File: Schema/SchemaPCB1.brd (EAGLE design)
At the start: 63.9 x 71.4 mm, 31 parts, among them J1 CON-HIROSE-COAXIAL-U.FL, J2 Programmer, J4 39700-0205, J5 39700-0002, U1 RN2483, U2 TPS22860DBVR, U3 ESP32, U4 SOT-89-5, U5 SI7217-B-01-IVR, U6 TPS22860DBVR

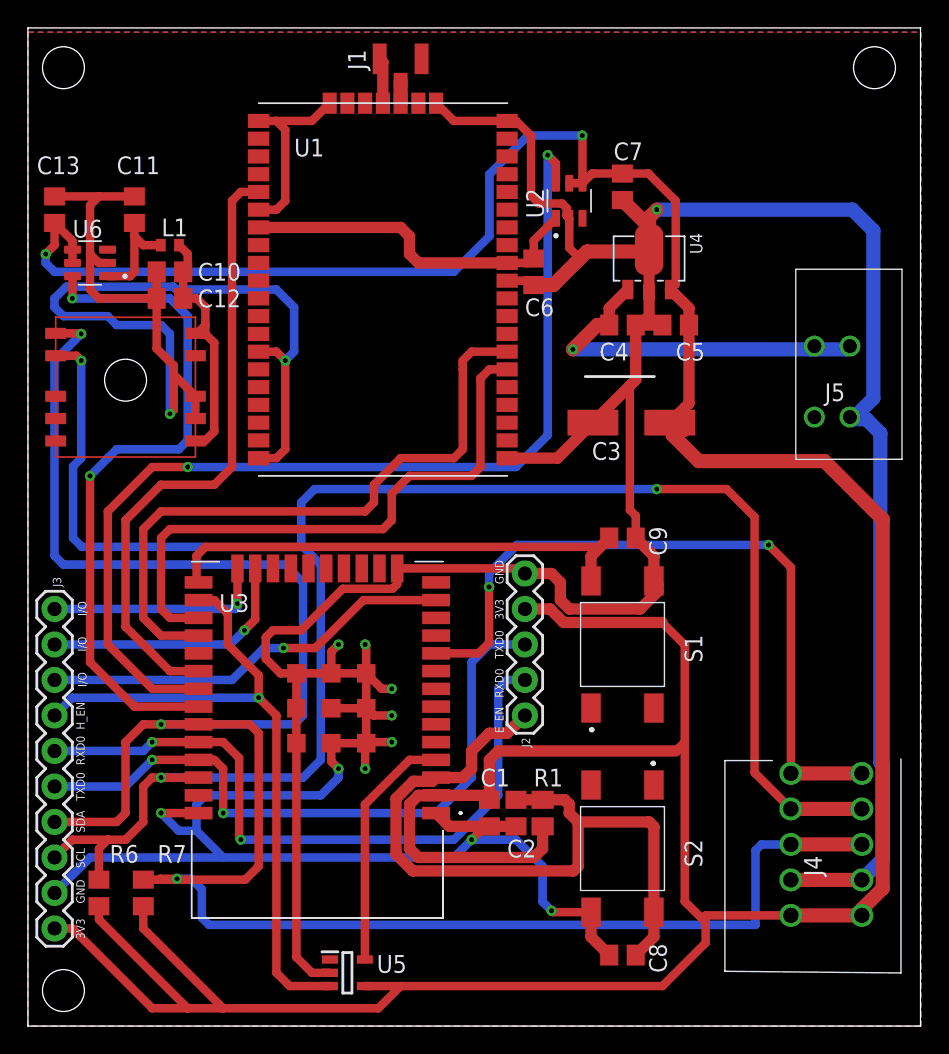
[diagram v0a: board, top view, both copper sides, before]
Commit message: aangepast om te gebruiken met gps breakout board
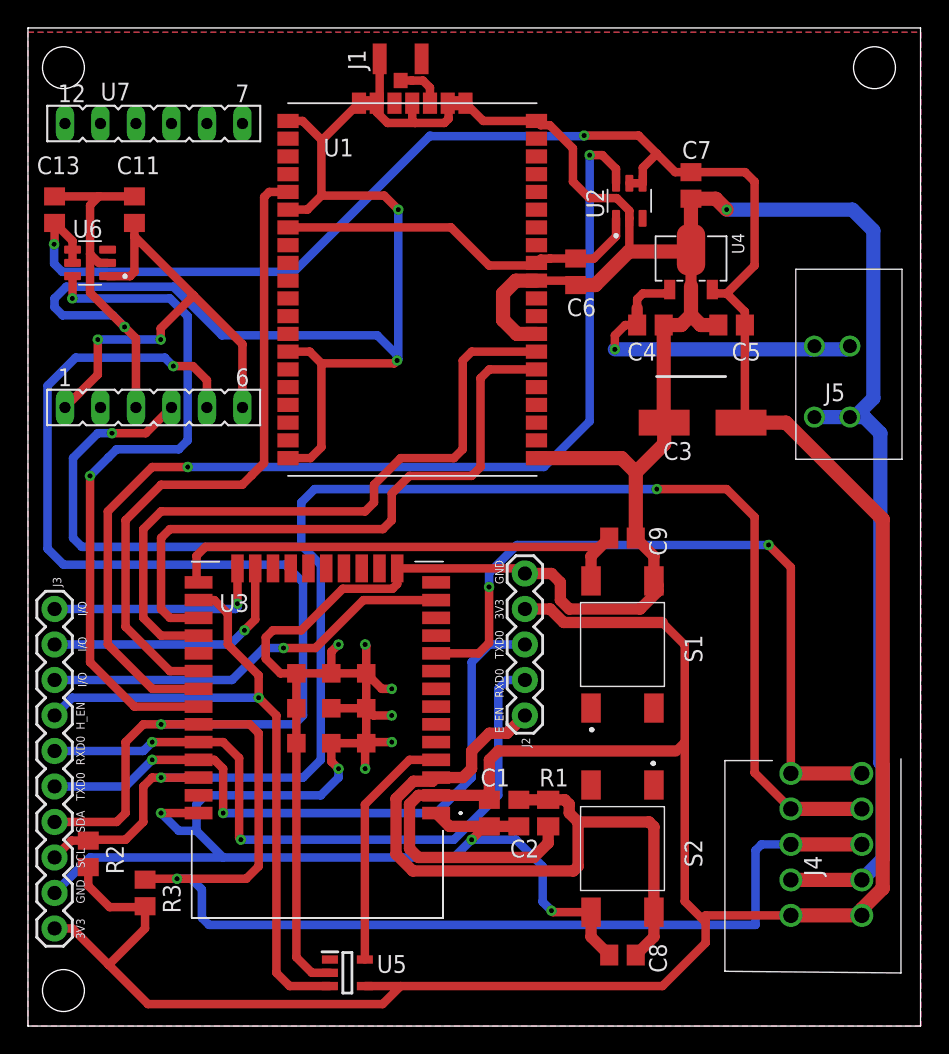
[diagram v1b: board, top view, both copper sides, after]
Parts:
- removed C10, C12: (no value), rcl:C0805
- removed L1: BLM15HB121SN1, inductors:0402
- removed R6, R7: (no value), rcl:R0805
- removed U?1: GPS, gps:GPS
- added R2, R3: (no value), rcl:R0805
- added U7: ADAFRUIT_MINIGPS, gps:ADAFRUIT_MINIGPS
- moved C3 5.10 mm to (48.3, 71.8)
- moved C7 4.90 mm to (47.4, 88.7)
- moved U2 4.30 mm to (43.0, 87.6)
- moved C5 4.00 mm to (50.4, 78.7)
- moved C6 3.00 mm to (39.2, 82.5)
- moved U4 3.00 mm to (47.5, 83.2)
- moved U1 2.10 mm to (18.6, 67.9)
- moved C4 2.00 mm to (44.5, 78.7)
- moved R1 0.40 mm to (37.2, 43.8)
- moved C2 0.20 mm to (35.1, 43.8)
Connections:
- removed net N$6: C10.1, C12.1, L1.1, U?1.NRESET, U?1.VCC
- removed net N$7: C11.1, L1.2, U6.1
- new net GPS_EN: C11.1, U6.1, U7.1, U7.6
- net +3V3: now also R2.2, R3.2; no longer R6.2, R7.2
- net GND: now also U7.3; no longer C10.2, C12.2, U?1.GND, U?1.WAKE-UP
- net I2C_SCL: now also R2.1, U7.4; no longer R6.1, U?1.I2C_SCL
- net I2C_SDA: now also R3.1, U7.5; no longer R7.1, U?1.I2C_SDA
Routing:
- net GPS_EN: track 0.00 -> 35.5 mm, vias 0 -> 2
- net GND: track 409.7 -> 437.7 mm, vias 13 -> 14
- net N$6: track 18.2 -> 0.00 mm
- net +3V3: track 287.7 -> 276.6 mm
- net N$7: track 7.70 -> 0.00 mm
- net I2C_SDA: track 154.3 -> 161.6 mm
- net I2C_SCL: track 140.5 -> 136.8 mm
- net RN2483_ENABLE: track 73.4 -> 76.9 mm
- net RXD2: track 42.6 -> 44.7 mm
- net TXD2: track 46.6 -> 48.7 mm
- net RN2483_RESET: track 44.6 -> 46.7 mm
- net BAT_IN: track 26.6 -> 24.6 mm
- net N$4: track 1.62 -> 3.43 mm
- net RN2483_VDD: track 25.1 -> 26.8 mm

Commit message: gerber files geexporteerd
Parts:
- C11: value (none) -> 100nF
- C13: value (none) -> 1uF
- R2, R3: value (none) -> 10k
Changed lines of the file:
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@@
 <attribute name="PURCHASE-URL" value="https://pricing.snapeda.com/search/part/TPS22860DBVR/?ref=eda" x="4.445" y="83.185" size="1.778" layer="27" rot="R180" display="off"/>
 </element>
-<element name="C11" library="rcl" library_urn="urn:adsk.eagle:library:334" package="C0805" package3d_urn="urn:adsk.eagle:package:23617/2" value="" x="7.62" y="86.995" smashed="yes" rot="R90">
+<element name="C11" library="rcl" library_urn="urn:adsk.eagle:library:334" package="C0805" package3d_urn="urn:adsk.eagle:package:23617/2" value="100nF" x="7.62" y="86.995" smashed="yes" rot="R90">
 <attribute name="NAME" x="6.35" y="89.535" size="1.27" layer="25"/>
 <attribute name="POPULARITY" value="88" x="7.62" y="86.995" size="1.778" layer="27" rot="R90" display="off"/>
@@
 <attribute name="VALUE" x="10.16" y="85.725" size="1.27" layer="27" rot="R90"/>
 </element>
-<element name="C13" library="rcl" library_urn="urn:adsk.eagle:library:334" package="C0805" package3d_urn="urn:adsk.eagle:package:23617/2" value="" x="1.905" y="86.995" smashed="yes" rot="R90">
+<element name="C13" library="rcl" library_urn="urn:adsk.eagle:library:334" package="C0805" package3d_urn="urn:adsk.eagle:package:23617/2" value="1uF" x="1.905" y="86.995" smashed="yes" rot="R90">
 <attribute name="NAME" x="0.635" y="89.535" size="1.27" layer="25"/>
 <attribute name="POPULARITY" value="88" x="1.905" y="86.995" size="1.778" layer="27" rot="R90" display="off"/>
@@
 <attribute name="NAME" x="57.7476" y="73.9314" size="1.27" layer="25" align="center"/>
 </element>
-<element name="R2" library="rcl" library_urn="urn:adsk.eagle:library:334" package="R0805" package3d_urn="urn:adsk.eagle:package:23553/2" value="" x="4.318" y="40.894" smashed="yes" rot="R270">
+<element name="R2" library="rcl" library_urn="urn:adsk.eagle:library:334" package="R0805" package3d_urn="urn:adsk.eagle:package:23553/2" value="10k" x="4.318" y="40.894" smashed="yes" rot="R270">
 <attribute name="NAME" x="5.588" y="41.529" size="1.27" layer="25" rot="R270"/>
 <attribute name="POPULARITY" value="86" x="4.318" y="40.894" size="1.778" layer="27" rot="R270" display="off"/>
@@
 <attribute name="VALUE" x="1.778" y="41.529" size="1.27" layer="27" rot="R270"/>
 </element>
-<element name="R3" library="rcl" library_urn="urn:adsk.eagle:library:334" package="R0805" package3d_urn="urn:adsk.eagle:package:23553/2" value="" x="8.382" y="38.1" smashed="yes" rot="R270">
+<element name="R3" library="rcl" library_urn="urn:adsk.eagle:library:334" package="R0805" package3d_urn="urn:adsk.eagle:package:23553/2" value="10k" x="8.382" y="38.1" smashed="yes" rot="R270">
 <attribute name="NAME" x="9.652" y="38.735" size="1.27" layer="25" rot="R270"/>
 <attribute name="POPULARITY" value="86" x="8.382" y="38.1" size="1.778" layer="27" rot="R270" display="off"/>
